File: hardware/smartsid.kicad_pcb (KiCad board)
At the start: 2 copper layers, 50.8 x 57.8 mm, 66 parts, among them P1 INPUT, P2 CONTROL, P3 POT2, P4 SOCKET LEFT, P5 OUTPUT, P6 SOCKET RIGHT, Q1 BC547, Q2 BC547, U1 GAL16V8, U2 SID2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

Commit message: Hardware: Adjusted regulator bypass cap values to 470p
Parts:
- C5, C7: value 330n -> 470p
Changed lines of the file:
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@@
 (kicad_pcb (version 4) (host pcbnew 4.0.0-rc2-stable)
   (general
-    (links 0)
+    (links 176)
     (no_connects 0)
-    (area 111.026448 53.665 202.666734 147.787)
+    (area 128.194999 67.234999 179.145001 125.170001)
     (thickness 1.6)
     (drawings 53)
@@
       (effects (font (size 1 1) (thickness 0.15)))
     )
-    (fp_text value 330n (at 0 -11.43 180) (layer F.Fab)
+    (fp_text value 470p (at 0 -11.43 180) (layer F.Fab)
       (effects (font (size 1 1) (thickness 0.15)))
     )
@@
       (effects (font (size 1 1) (thickness 0.15)))
     )
-    (fp_text value 330n (at 0 -14.478 180) (layer F.Fab)
-      (effects (font (size 1 1) (thickness 0.15)))
-    )
+    (fp_text value 470p (at 0 -14.478 180) (layer F.Fab)
+      (effects (font (size 1 1) (thickness 0.15)))
+    )

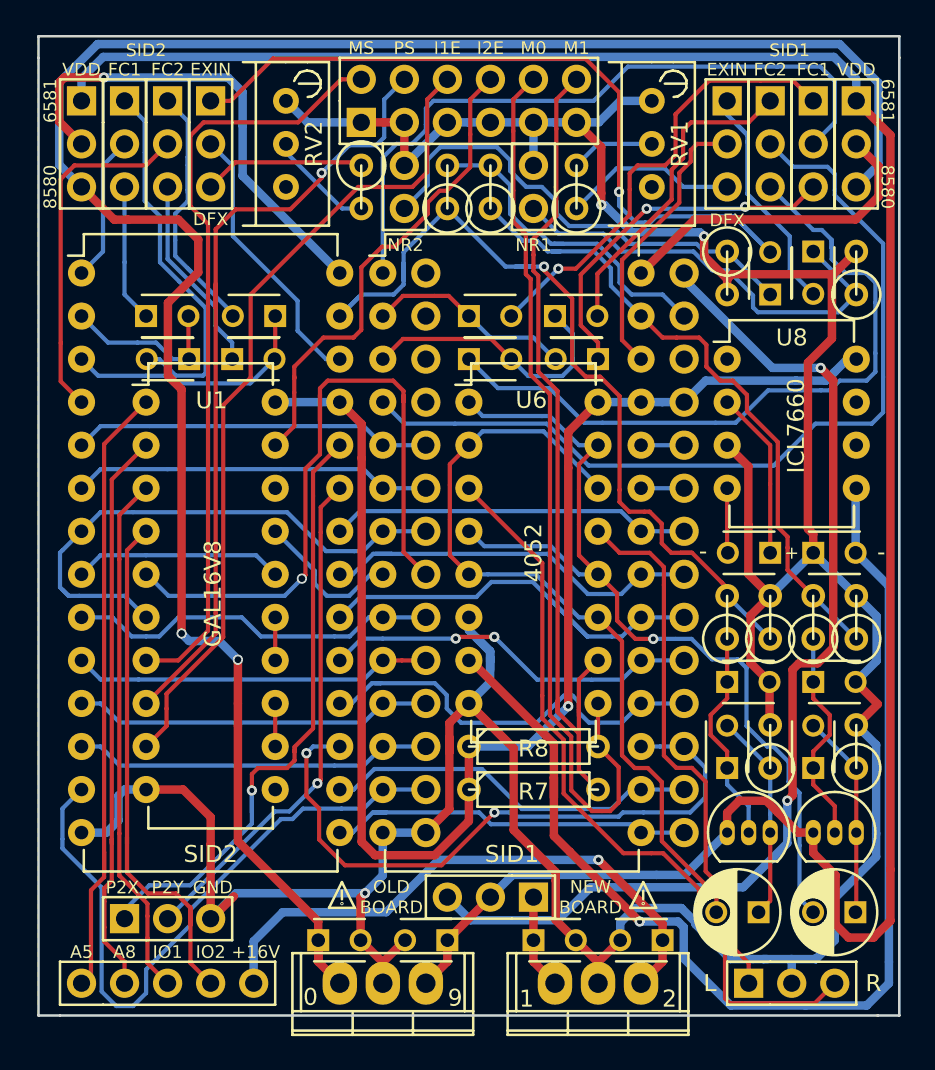
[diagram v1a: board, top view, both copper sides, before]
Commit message: Hardware: Reordered filter caps for SID2 (consistency)
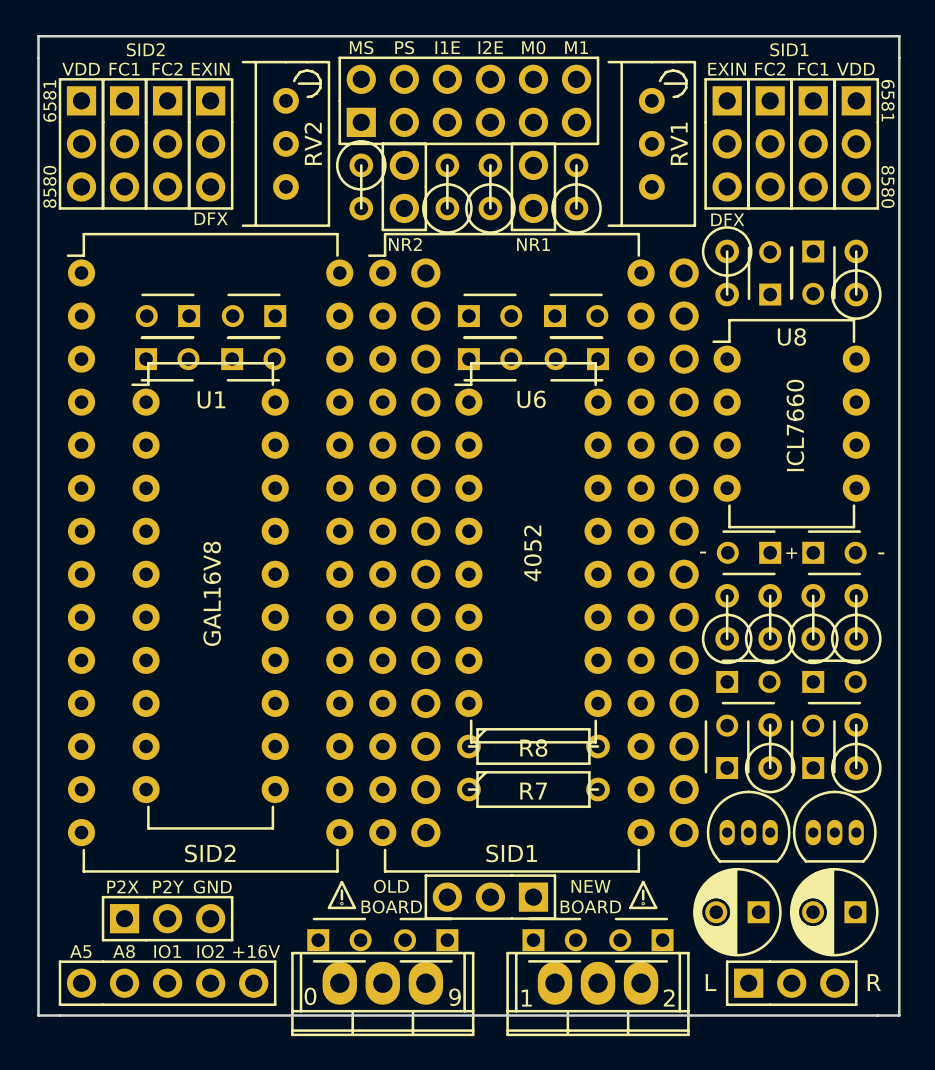
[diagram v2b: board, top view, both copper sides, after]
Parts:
- moved C3 2.54 mm to (137.2, 83.8)
- moved C4 2.54 mm to (134.6, 86.4)
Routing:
- net GND: track 223.1 -> 0.00 mm, vias 3 -> 0
- net /+12V: track 138.1 -> 0.00 mm
- net /+9V: track 122.8 -> 0.00 mm, vias 2 -> 0
- net VCC: track 86.5 -> 0.00 mm, vias 1 -> 0
- net /VEE: track 69.3 -> 0.00 mm, vias 1 -> 0
- net VDD: track 63.2 -> 0.00 mm, vias 2 -> 0
- net /LEFT: track 54.2 -> 0.00 mm, vias 1 -> 0
- net /M1: track 53.7 -> 0.00 mm
- net /M0: track 52.7 -> 0.00 mm
- net Net-(JP6-Pad2): track 52.2 -> 0.00 mm
- net /S2OUT: track 51.6 -> 0.00 mm, vias 1 -> 0
- net /IO1EN: track 48.6 -> 0.00 mm
- net /RIGHT: track 47.4 -> 0.00 mm
- net /PS: track 47.4 -> 0.00 mm, vias 1 -> 0
- net /MS: track 45.6 -> 0.00 mm
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- removed copper zone on B.Cu, net GND
- removed copper zone on F.Cu, net GND

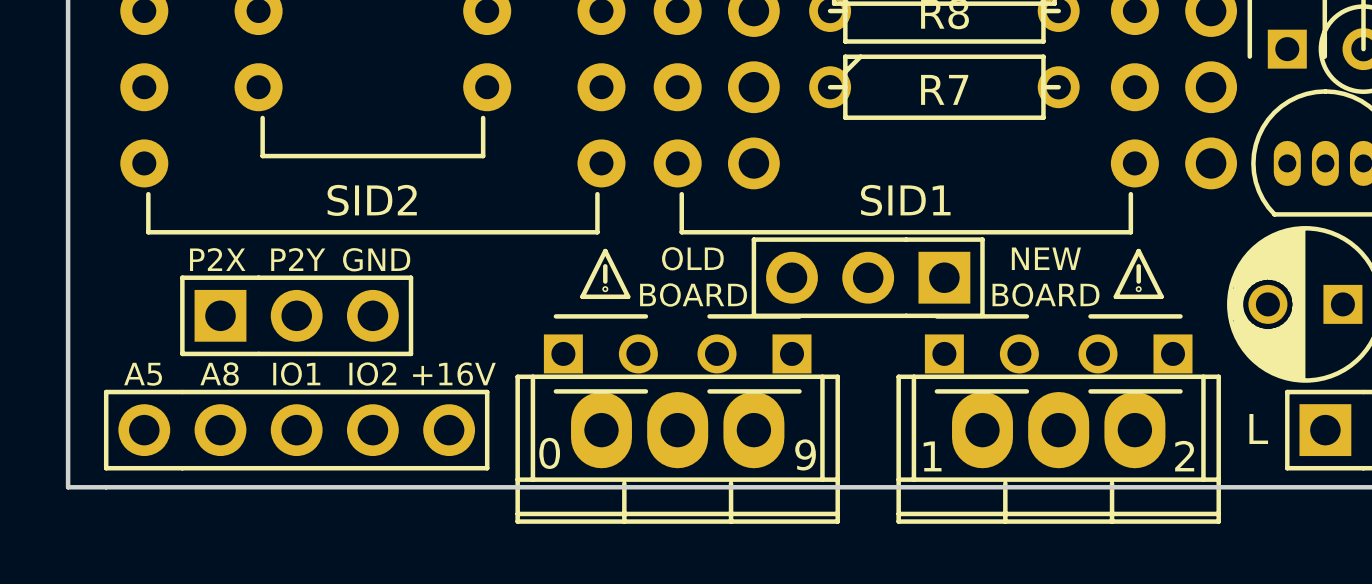
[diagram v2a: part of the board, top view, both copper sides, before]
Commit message: Hardware: Removed SID2 pot connector, moved board select jumper
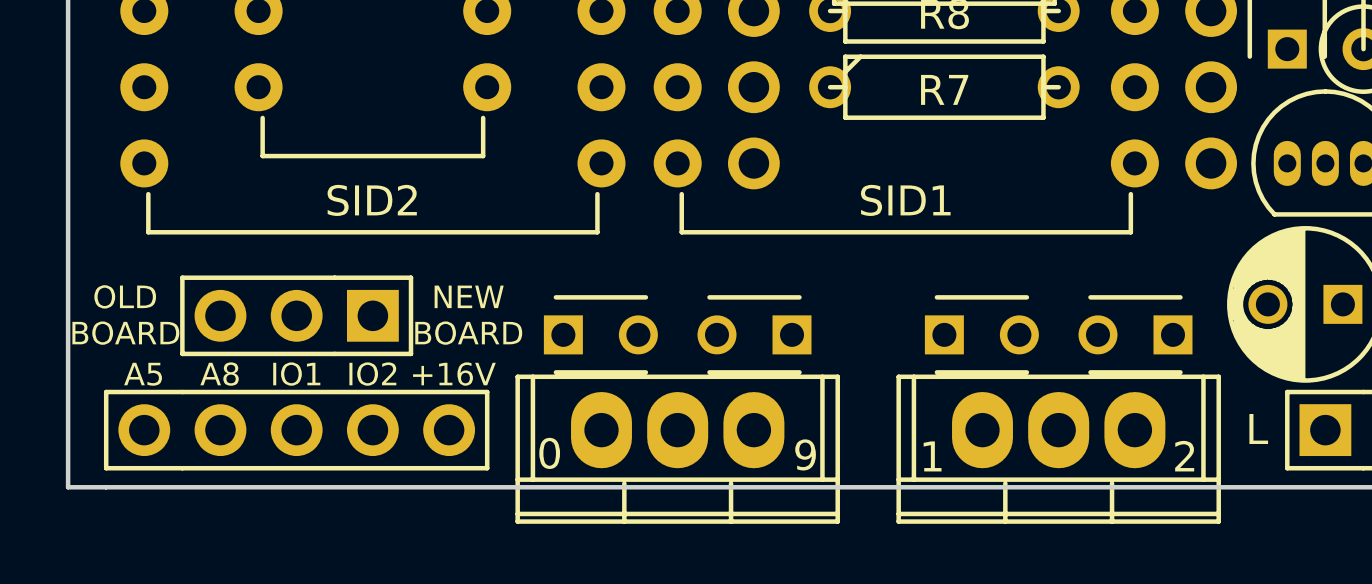
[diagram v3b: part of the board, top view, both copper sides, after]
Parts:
- removed P3: POT2, Pinheaders:Pin_Header_Straight_1x03
- removed REF** (x2): Attention, Pinheaders:Attention
- moved JP4 19.1 mm to (138.4, 119.4)
- moved C5 0.64 mm to (165.1, 120.0)
- moved C6 0.64 mm to (157.5, 120.0)
- moved C7 0.64 mm to (152.4, 120.0)
- moved C8 0.64 mm to (144.8, 120.0)
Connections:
- U2 pad 23: /POT2Y -> GND
- U2 pad 24: /POT2X -> GND
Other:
- board text removed: "GND"
- board text removed: "P2X"
- board text removed: "P2Y"

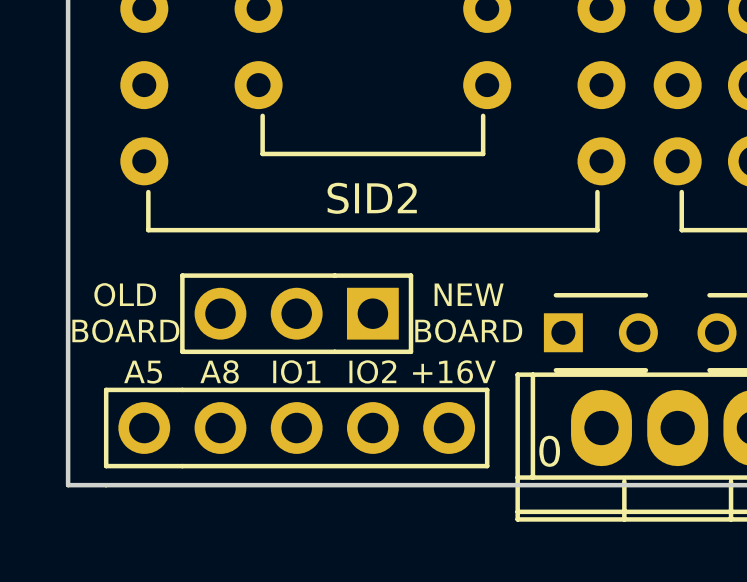
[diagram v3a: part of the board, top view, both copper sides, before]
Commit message: Hardware: Renamed +16V line to VEXT, improved silk screen
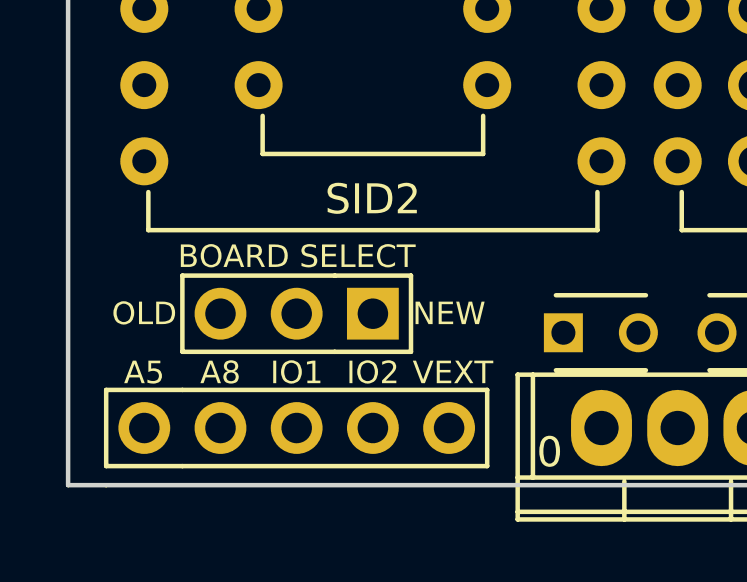
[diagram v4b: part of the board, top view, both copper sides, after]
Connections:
- net /+16V renamed /VEXT
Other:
- board text added: "BOARD SELECT"
- board text added: "NEW"
- board text added: "OLD"
- board text added: "VEXT"
- board text removed: "+16V"
- board text removed: "NEW BOARD"
- board text removed: "OLD BOARD"

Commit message: Hardware: Corrected order of SIDs on audio channels, default mix setting
Now the left sid appears on the left channel and the right sid on the right
channel. Also the default mix state (without driving M0 and M1) has been
changed to Left/Right. This should match expectations.
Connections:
- C19 pad 2: /RIGHT -> /LEFT
- C22 pad 2: /LEFT -> /RIGHT
- U6 pad 11: /RIGHT -> /LEFT
- U6 pad 15: /LEFT -> /RIGHT
- U6 pad 2: /RIGHT -> /LEFT
- U6 pad 4: /LEFT -> /RIGHT
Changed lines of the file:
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@@
     (pad_to_mask_clearance 0.2)
     (aux_axis_origin 0 0)
-    (visible_elements 7FFFFFFF)
+    (visible_elements 7FFFF7FF)
     (pcbplotparams
       (layerselection 0x010e0_00000001)
@@
       (net 62 /LEFT))
     (pad 2 thru_hole oval (at 0 2.54) (size 1.6 1.6) (drill 0.8) (layers *.Cu *.Mask F.SilkS)
-      (net 63 /RIGHT))
+      (net 62 /LEFT))
     (pad 3 thru_hole oval (at 0 5.08) (size 1.6 1.6) (drill 0.8) (layers *.Cu *.Mask F.SilkS)
       (net 72 /RIGHT_OUT))
     (pad 4 thru_hole oval (at 0 7.62) (size 1.6 1.6) (drill 0.8) (layers *.Cu *.Mask F.SilkS)
-      (net 62 /LEFT))
+      (net 63 /RIGHT))
     (pad 5 thru_hole oval (at 0 10.16) (size 1.6 1.6) (drill 0.8) (layers *.Cu *.Mask F.SilkS)
       (net 63 /RIGHT))
@@
       (net 65 /M0))
     (pad 11 thru_hole oval (at 7.62 12.7) (size 1.6 1.6) (drill 0.8) (layers *.Cu *.Mask F.SilkS)
-      (net 63 /RIGHT))
+      (net 62 /LEFT))
     (pad 12 thru_hole oval (at 7.62 10.16) (size 1.6 1.6) (drill 0.8) (layers *.Cu *.Mask F.SilkS)
       (net 62 /LEFT))
@@
       (net 63 /RIGHT))
     (pad 15 thru_hole oval (at 7.62 2.54) (size 1.6 1.6) (drill 0.8) (layers *.Cu *.Mask F.SilkS)
-      (net 62 /LEFT))
+      (net 63 /RIGHT))
     (pad 16 thru_hole oval (at 7.62 0) (size 1.6 1.6) (drill 0.8) (layers *.Cu *.Mask F.SilkS)
       (net 33 VCC))
@@
       (net 64 "Net-(C16-Pad2)"))
     (pad 2 thru_hole circle (at 2.5 0 180) (size 1.3 1.3) (drill 0.8) (layers *.Cu *.Mask F.SilkS)
-      (net 63 /RIGHT))
+      (net 62 /LEFT))
     (model Capacitors_ThroughHole.3dshapes/C_Radial_D5_L6_P2.5.wrl
       (at (xyz 0.049213 0 0))
@@
       (net 88 "Net-(C21-Pad2)"))
     (pad 2 thru_hole circle (at 2.5 0 180) (size 1.3 1.3) (drill 0.8) (layers *.Cu *.Mask F.SilkS)
-      (net 62 /LEFT))
+      (net 63 /RIGHT))
     (model Capacitors_ThroughHole.3dshapes/C_Radial_D5_L6_P2.5.wrl
       (at (xyz 0.049213 0 0))

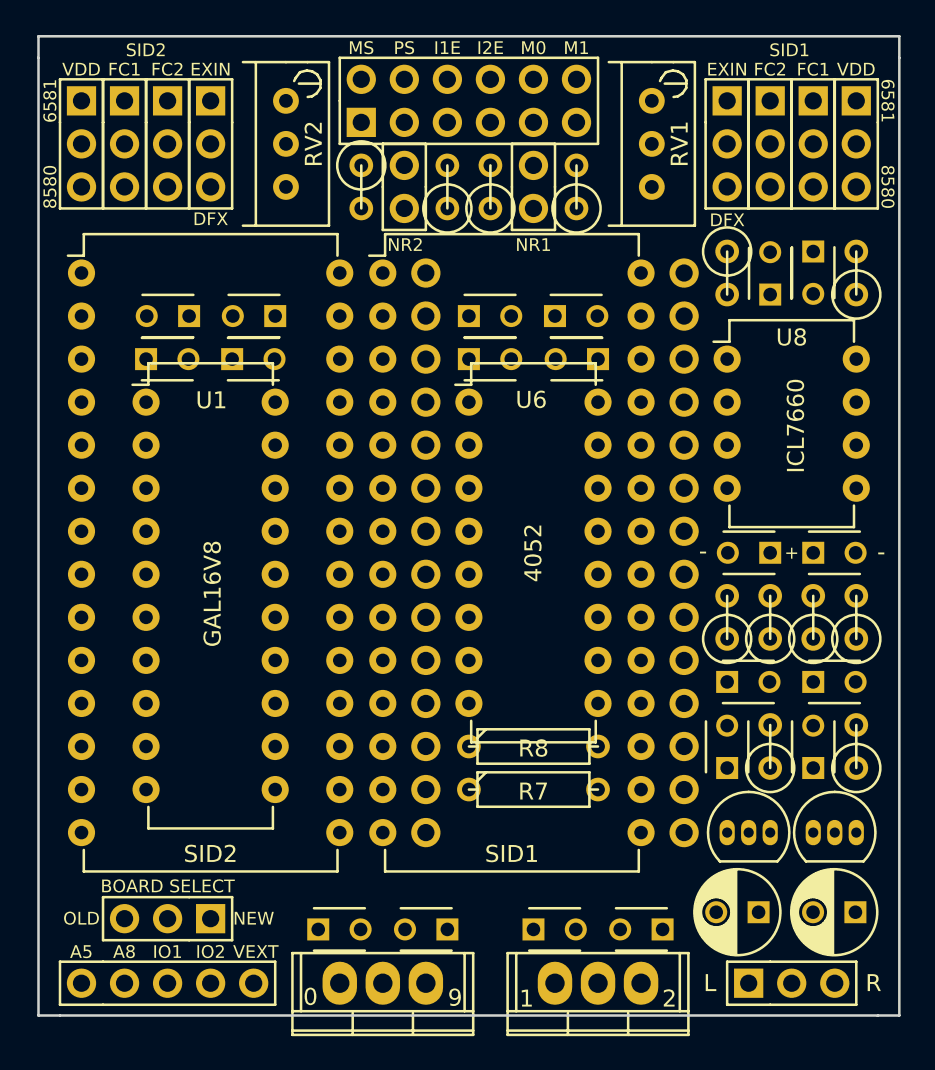
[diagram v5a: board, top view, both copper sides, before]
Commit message: Hardware: Removed priority select, rearranged GAL pin layout
Switching SID priorities does not seem very useful and will break paddles
when priority is swapped in stereo addressing mode.
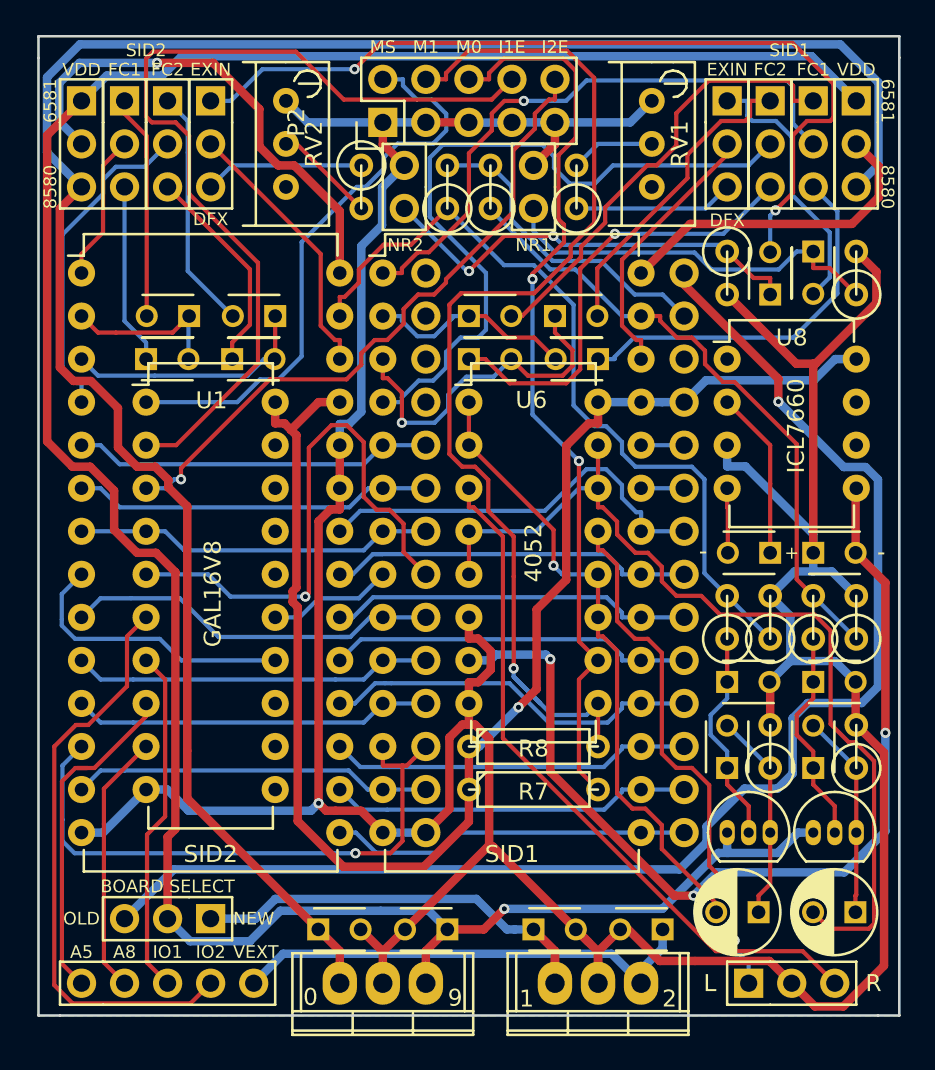
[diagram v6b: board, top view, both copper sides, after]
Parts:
- P2: footprint Pinheaders:Pin_Header_Straight_2x06 -> Pin_Headers:Pin_Header_Straight_2x05
- moved P2 1.27 mm to (148.6, 72.4)
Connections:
- P2 pad 10: /M1 -> /~IO2EN
- P2 pad 4: /PS -> /M1
- P2 pad 6: /IO1EN -> /M0
- P2 pad 8: /IO2EN -> /~IO1EN
- U1 pad 1: /A5 -> /MS
- U1 pad 13: Net-(U1-Pad12) -> Net-(U1-Pad13)
- U1 pad 14: Net-(U1-Pad14) -> /~CS2
- U1 pad 15: Net-(U1-Pad14) -> /~CS1
- U1 pad 16: /~CS2 -> Net-(U1-Pad16)
- U1 pad 17: /~CS1 -> Net-(U1-Pad17)
- U1 pad 19: /IO2EN -> Net-(U1-Pad19)
- U1 pad 2: /A8 -> /~IO1EN
- U1 pad 3: /~IO1 -> /~IO2EN
- U1 pad 4: /~IO2 -> /RW
- U1 pad 6: /RW -> /~IO2
- U1 pad 7: /MS -> /~IO1
- U1 pad 8: /PS -> /A5
- U1 pad 9: /IO1EN -> /A8
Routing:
- net GND: track 0.00 -> 235.7 mm, vias 0 -> 1
- net /+12V: track 0.00 -> 149.4 mm, vias 0 -> 1
- net /+9V: track 0.00 -> 120.4 mm
- net VCC: track 0.00 -> 86.5 mm, vias 0 -> 1
- net VDD: track 0.00 -> 82.5 mm, vias 0 -> 1
- net /M1: track 0.00 -> 65.9 mm, vias 0 -> 1
- net /VEE: track 0.00 -> 57.1 mm, vias 0 -> 3
- net /RIGHT: track 0.00 -> 55.3 mm
- net /M0: track 0.00 -> 53.6 mm, vias 0 -> 2
- net /~IO1EN: track 0.00 -> 53.6 mm
- net Net-(C13-Pad2): track 0.00 -> 51.4 mm, vias 0 -> 2
- net /S2OUT: track 0.00 -> 46.8 mm
- net Net-(JP6-Pad2): track 0.00 -> 42.8 mm
- net /RIGHT_OUT: track 0.00 -> 41.3 mm
- net /~IO2EN: track 0.00 -> 38.9 mm, vias 0 -> 1
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- added copper zone on B.Cu, net GND
- added copper zone on F.Cu, net GND
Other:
- board text removed: "PS"
